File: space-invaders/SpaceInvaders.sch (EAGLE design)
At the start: 26 parts, among them J2-J4 TM4C123GXL, J3-J1 TM4C123GXL, J5 NOKIA_5110, J6 NOKIA_5110, J7 9V, U1 LM7805CT

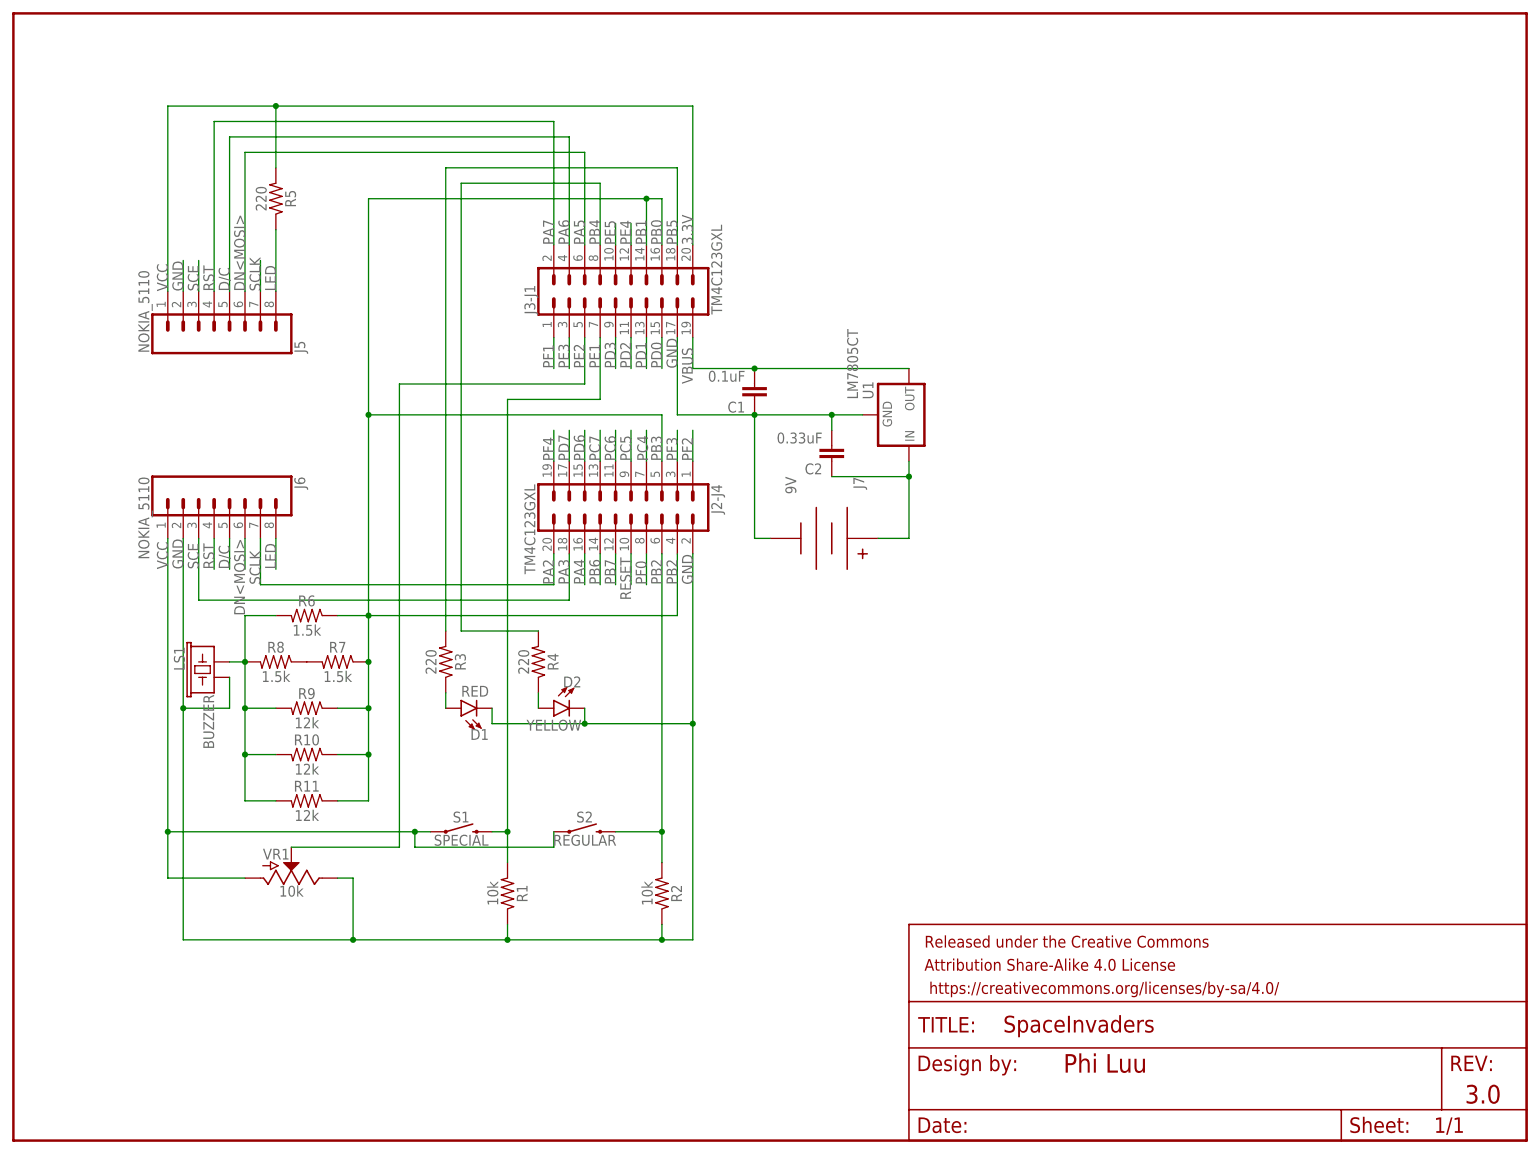
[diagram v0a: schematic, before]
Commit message: Expand & make more space in schematic
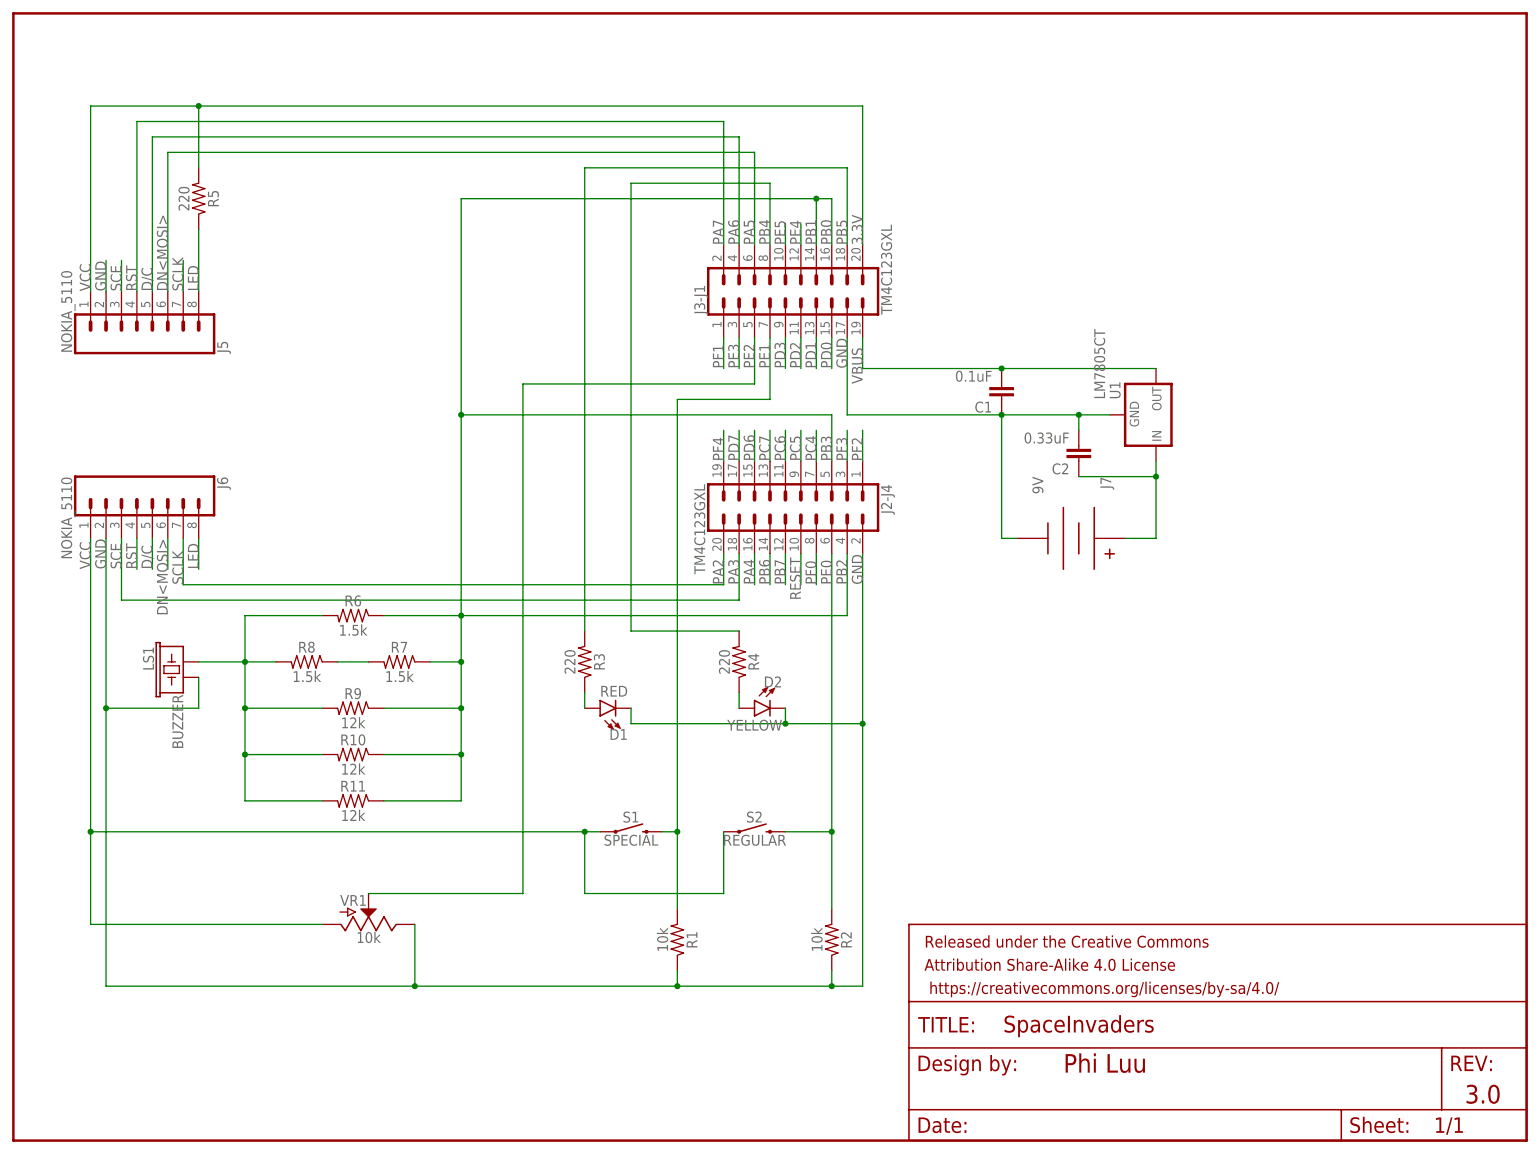
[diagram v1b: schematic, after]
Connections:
- net PB2 renamed PE0
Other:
- note added: "PB2"
- moved on the sheet: C1, C2, D1, D2, J2-J4, J3-J1, J5, J6, J7, LS1, R1, R10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
